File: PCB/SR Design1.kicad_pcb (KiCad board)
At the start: 2 copper layers, 53.3 x 94 mm, 5 parts, among them J1 IMU (I2C), J2 GPS (UART), J3 BT (UART), J4 SD (SPI)

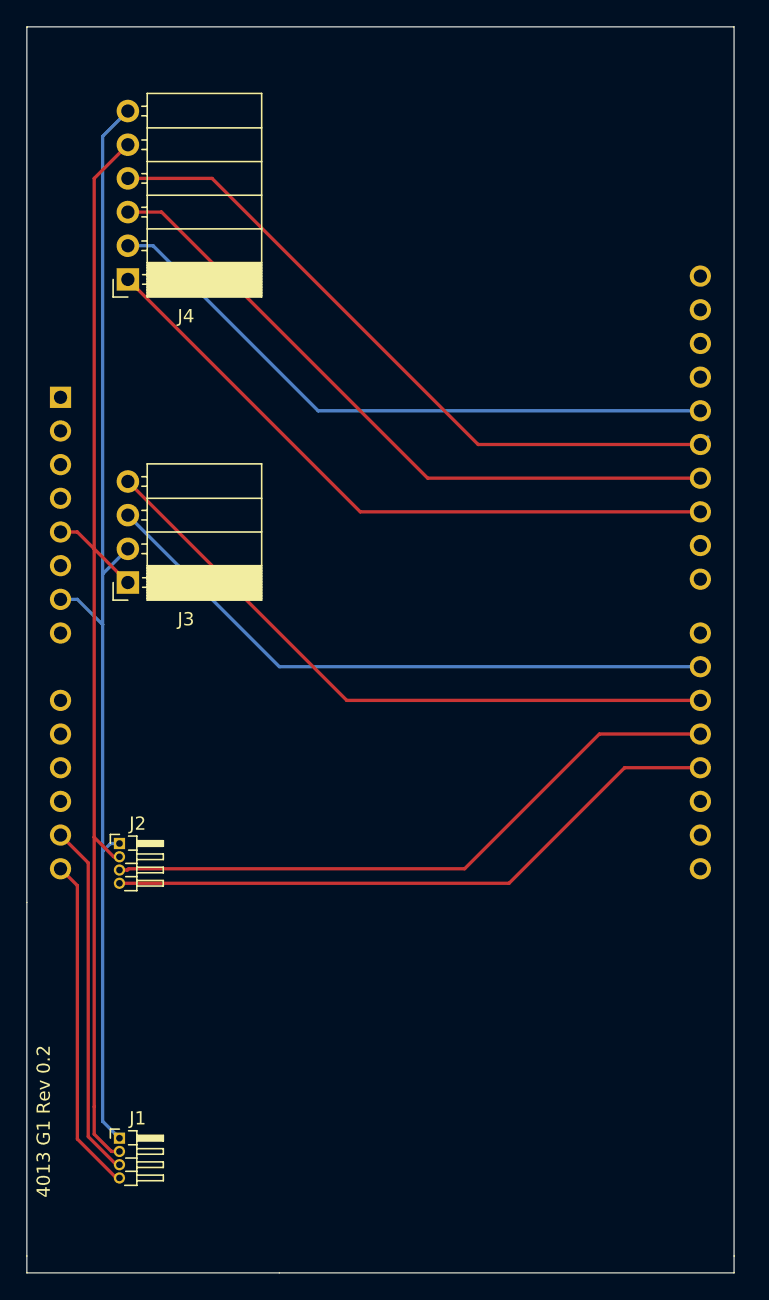
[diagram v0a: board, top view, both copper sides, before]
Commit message: Updated PCB to REV 0.3
Updated all PCB files previously added. These should be updated to Rev 0.3 with new BT module and alternative power circuit. Board size not changed.
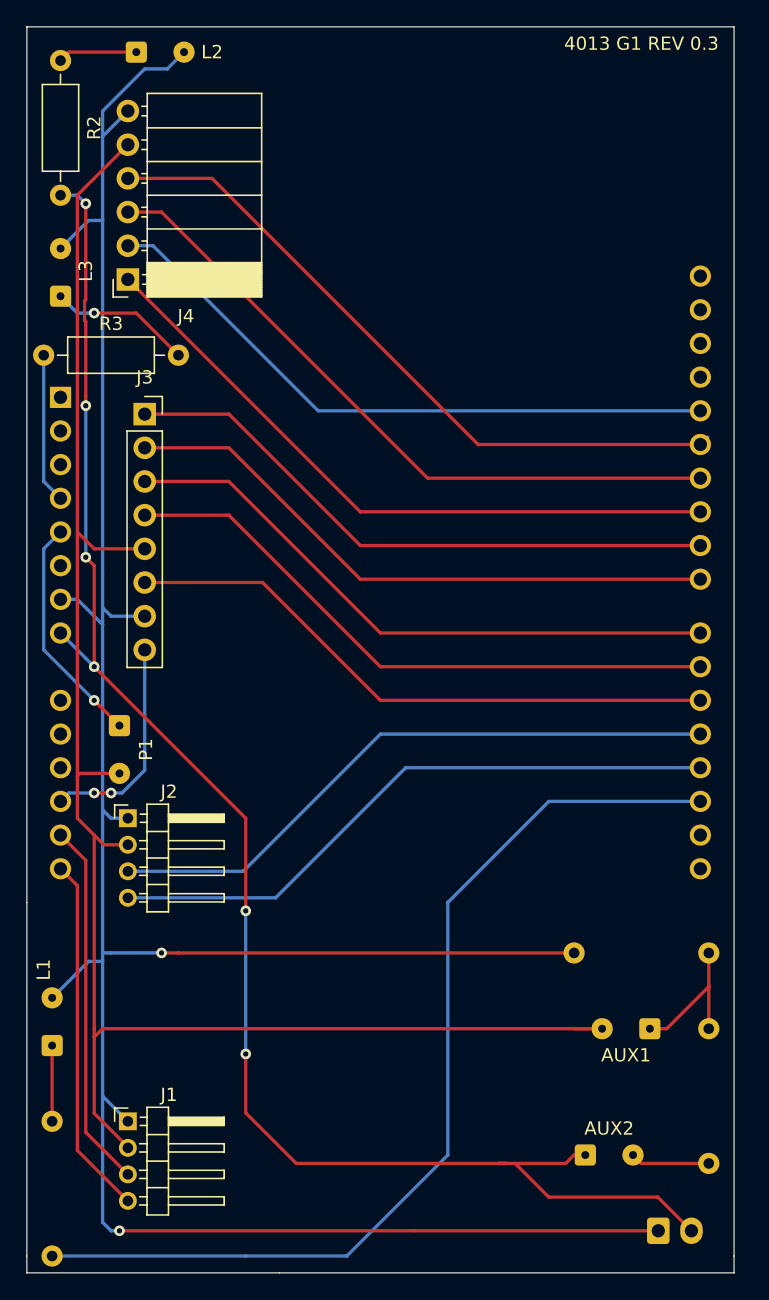
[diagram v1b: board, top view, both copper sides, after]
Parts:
- added AUX1: PWR, Connector_Wire:SolderWire-0.1sqmm_1x02_P3.6mm_D0.4mm_OD1mm, F.Cu at (137.2, 140.3)
- added AUX2: PWR, Connector_Wire:SolderWire-0.1sqmm_1x02_P3.6mm_D0.4mm_OD1mm, F.Cu at (132.3, 149.9)
- added Batt1: PWR, Connector_JST:JST_XH_B2B-XH-A_1x02_P2.50mm_Vertical, B.Cu at (137.8, 155.6)
- added L1: LED, Connector_Wire:SolderWire-0.1sqmm_1x02_P3.6mm_D0.4mm_OD1mm, F.Cu at (92.1, 141.6)
- added L2: LED, Connector_Wire:SolderWire-0.1sqmm_1x02_P3.6mm_D0.4mm_OD1mm, F.Cu at (98.4, 66.7)
- added L3: LED, Connector_Wire:SolderWire-0.1sqmm_1x02_P3.6mm_D0.4mm_OD1mm, F.Cu at (92.7, 85.1)
- added P1: PWR, Connector_Wire:SolderWire-0.1sqmm_1x02_P3.6mm_D0.4mm_OD1mm, F.Cu at (97.2, 117.5)
- added R1: R227, Resistor_THT:R_Axial_DIN0207_L6.3mm_D2.5mm_P10.16mm_Horizontal, B.Cu at (92.1, 157.5)
- added R2: R227, Resistor_THT:R_Axial_DIN0207_L6.3mm_D2.5mm_P10.16mm_Horizontal, F.Cu at (92.7, 77.5)
- added R3: R227, Resistor_THT:R_Axial_DIN0207_L6.3mm_D2.5mm_P10.16mm_Horizontal, F.Cu at (91.4, 89.5)
- added R4: R5k, Resistor_THT:R_Axial_DIN0207_L6.3mm_D2.5mm_P10.16mm_Horizontal, B.Cu at (131.4, 134.6)
- added R5: R2.2k, Resistor_THT:R_Axial_DIN0207_L6.3mm_D2.5mm_P10.16mm_Horizontal, B.Cu at (141.6, 140.3)
- J1, J2: footprint Connector_PinHeader_1.00mm:PinHeader_1x04_P1.00mm_Horizontal -> Connector_PinHeader_2.00mm:PinHeader_1x04_P2.00mm_Horizontal
- J3: value BT (UART) -> BT (UART +); footprint Connector_PinSocket_2.54mm:PinSocket_1x04_P2.54mm_Horizontal -> Connector_PinSocket_2.54mm:PinSocket_1x08_P2.54mm_Vertical
- moved J3 12.8 mm to (99.1, 94.0), turned to 0 degrees
- moved J2 2.01 mm to (97.8, 124.5)
- moved J1 1.42 mm to (97.8, 147.3)
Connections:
- J1 pad 2: Net-(A1-Pad5) -> Net-(AUX1-Pad2)
- J2 pad 2: Net-(A1-Pad5) -> Net-(AUX1-Pad2)
- J3 pad 1: Net-(A1-Pad5) -> Net-(A1-Pad24)
- J3 pad 2: Net-(A1-Pad7) -> Net-(A1-Pad23)
- J3 pad 3: Net-(A1-Pad21) -> Net-(A1-Pad22)
- J3 pad 4: Net-(A1-Pad20) -> Net-(A1-Pad21)
- J4 pad 5: Net-(A1-Pad5) -> Net-(AUX1-Pad2)
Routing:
- net Net-(AUX1-Pad2): track 0.00 -> 131.2 mm
- net Net-(A1-Pad8): track 0.00 -> 123.5 mm, vias 0 -> 6
- net Net-(A1-Pad7): track 87.0 -> 193.5 mm, vias 0 -> 2
- net Net-(A1-Pad17): track 0.00 -> 74.3 mm
- net Net-(A1-Pad5): track 87.3 -> 17.5 mm, vias 0 -> 1
- net Net-(A1-Pad22): track 0.00 -> 46.6 mm
- net Net-(A1-Pad23): track 0.00 -> 46.0 mm
- net Net-(A1-Pad24): track 0.00 -> 46.0 mm
- net Net-(A1-Pad12): track 0.00 -> 16.4 mm, vias 0 -> 2
- net Net-(AUX1-Pad1): track 0.00 -> 11.5 mm
- net Net-(A1-Pad4): track 0.00 -> 11.3 mm
- net Net-(L3-Pad1): track 0.00 -> 10.7 mm, vias 0 -> 1
- net Net-(L2-Pad1): track 0.00 -> 5.98 mm
- net Net-(AUX2-Pad2): track 0.00 -> 5.98 mm
- net Net-(L1-Pad1): track 0.00 -> 5.72 mm
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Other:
- board text added: "4013 G1 REV 0.3"
- board text removed: "4013 G1 Rev 0.2"
